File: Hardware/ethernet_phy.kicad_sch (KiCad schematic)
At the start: 28 parts, among them J5 WE-RJ45_7499010211A, U5 DP83822IRHBR

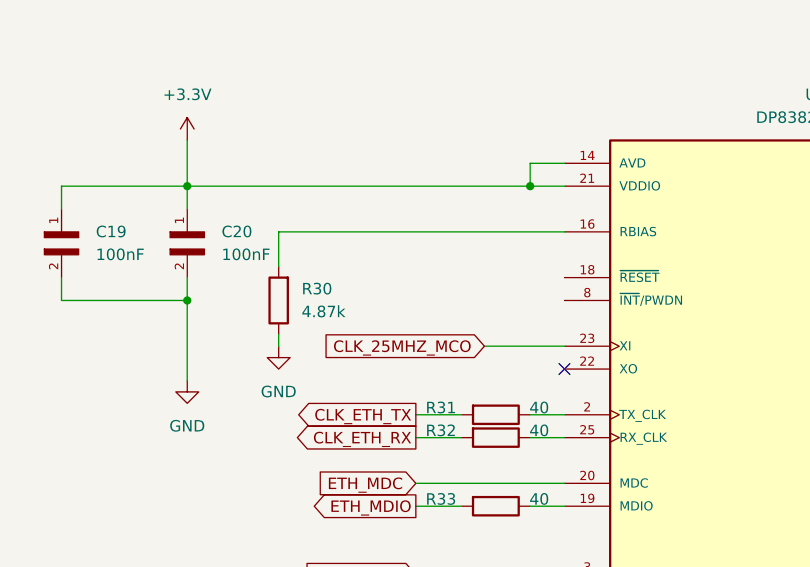
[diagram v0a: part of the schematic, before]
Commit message: Added oscillators, reset button, and finalized ETH connection
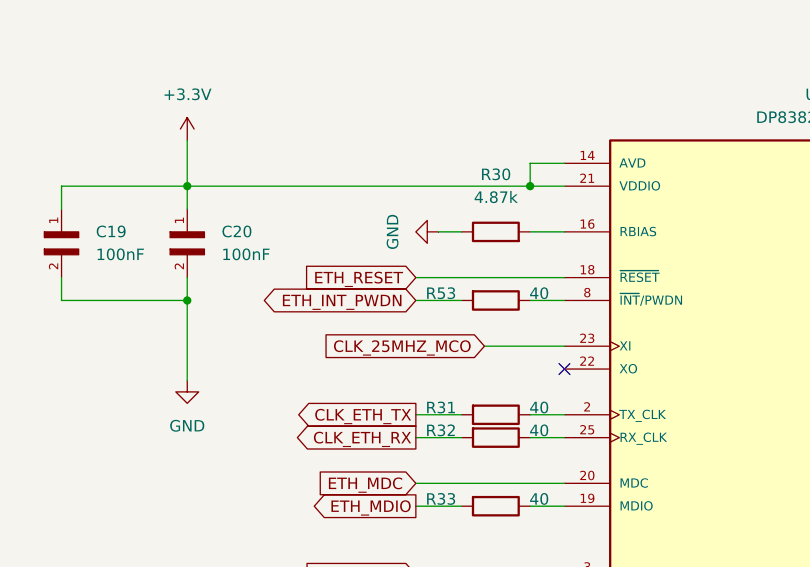
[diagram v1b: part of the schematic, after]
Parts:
- added R53: 40, Resistor_SMD:R_0402_1005Metric, symbol Device:R
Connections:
- net ETH_RESET: now reaches U5.18 (~{RESET})
- net at U5.8 (~{INT}/PWDN): now also R53.1
- new net ETH_INT_PWDN: R53.2
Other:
- company: (none) -> Thomas Montano
- title: (none) -> Ethernet PHY Interface
- moved on the sheet: R30
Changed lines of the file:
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@@
 	(generator_version "9.0")
 	(paper "A4")
+	(title_block
+		(title "Ethernet PHY Interface")
+		(date "2025-06-25")
+		(rev "1")
+		(company "Thomas Montano")
+	)
 	(text "Bias Resistor Connection: A 4.87-kΩ ±1% resistor must be connected \nfrom RBIAS to GND."
 		(exclude_from_sim no)
@@
 	(wire
 		(pts
-			(xy 134.62 123.19) (xy 134.62 125.73)
+			(xy 57.15 54.61) (xy 73.66 54.61)
 		)
 		(stroke
@@
 	(wire
 		(pts
-			(xy 41.91 60.96) (xy 41.91 62.23)
+			(xy 134.62 123.19) (xy 134.62 125.73)
 		)
 		(stroke
@@
 	(wire
 		(pts
+			(xy 69.85 57.15) (xy 73.66 57.15)
+		)
+		(stroke
+			(width 0)
+			(type default)
+		)
+	)
+	(wire
+		(pts
 			(xy 227.33 74.93) (xy 227.33 80.01)
 		)
@@
 	(wire
 		(pts
-			(xy 134.62 133.35) (xy 134.62 137.16)
+			(xy 62.23 49.53) (xy 59.69 49.53)
 		)
 		(stroke
@@
 	(wire
 		(pts
-			(xy 163.83 62.23) (xy 163.83 45.72)
+			(xy 134.62 133.35) (xy 134.62 137.16)
 		)
 		(stroke
@@
 	(wire
 		(pts
-			(xy 129.54 50.8) (xy 148.59 50.8)
+			(xy 163.83 62.23) (xy 163.83 45.72)
 		)
 		(stroke
@@
 	(wire
 		(pts
-			(xy 129.54 53.34) (xy 142.24 53.34)
+			(xy 129.54 50.8) (xy 148.59 50.8)
 		)
 		(stroke
@@
 	(wire
 		(pts
-			(xy 270.51 83.82) (xy 274.32 83.82)
+			(xy 129.54 53.34) (xy 142.24 53.34)
 		)
 		(stroke
@@
 	(wire
 		(pts
-			(xy 163.83 38.1) (xy 163.83 43.18)
+			(xy 270.51 83.82) (xy 274.32 83.82)
 		)
 		(stroke
@@
 	(wire
 		(pts
-			(xy 57.15 97.79) (xy 73.66 97.79)
+			(xy 163.83 38.1) (xy 163.83 43.18)
 		)
 		(stroke
@@
 	(wire
 		(pts
-			(xy 134.62 130.81) (xy 134.62 133.35)
+			(xy 57.15 97.79) (xy 73.66 97.79)
 		)
 		(stroke
@@
 	(wire
 		(pts
-			(xy 41.91 53.34) (xy 41.91 49.53)
+			(xy 134.62 130.81) (xy 134.62 133.35)
 		)
 		(stroke
@@
 	(wire
 		(pts
+			(xy 57.15 57.15) (xy 62.23 57.15)
+		)
+		(stroke
+			(width 0)
+			(type default)
+		)
+	)
+	(wire
+		(pts
 			(xy 73.66 44.45) (xy 69.85 44.45)
 		)
@@
 	(wire
 		(pts
-			(xy 41.91 49.53) (xy 73.66 49.53)
+			(xy 69.85 49.53) (xy 73.66 49.53)
 		)
 		(stroke
@@
 		)
 	)
+	(global_label "ETH_INT_PWDN"
+		(shape bidirectional)
+		(at 57.15 57.15 180)
+		(fields_autoplaced yes)
+		(effects
+			(font
+				(size 1.27 1.27)
+			)
+			(justify right)
+		)
+		(property "Intersheetrefs" "${INTERSHEET_REFS}"
+			(at 45.7587 57.15 0)
+			(effects
+				(font
+					(size 1.27 1.27)
+				)
+				(justify right)
+				(hide yes)
+			)
+		)
+	)
 	(global_label "ETH_RX_CRS"
 		(shape output)
@@
 		)
 	)
+	(global_label "ETH_RESET"
+		(shape input)
+		(at 57.15 54.61 180)
+		(fields_autoplaced yes)
+		(effects
+			(font
+				(size 1.27 1.27)
+			)
+			(justify right)
+		)
+		(property "Intersheetrefs" "${INTERSHEET_REFS}"
+			(at 45.7587 54.61 0)
+			(effects
+				(font
+					(size 1.27 1.27)
+				)
+				(justify right)
+				(hide yes)
+			)
+		)
+	)
 	(global_label "ETH_RX_D0"
 		(shape output)
@@
 	(symbol
 		(lib_id "power:GND")
-		(at 41.91 62.23 0)
+		(at 59.69 49.53 270)
 		(unit 1)
 		(exclude_from_sim no)
@@
 		(dnp no)
 		(property "Reference" "#PWR036"
-			(at 41.91 68.58 0)
+			(at 53.34 49.53 0)
 			(effects
 				(font
@@
 		)
 		(property "Value" "GND"
-			(at 41.91 67.31 0)
+			(at 54.61 49.53 0)
 			(effects
 				(font
@@
 		)
 		(property "Footprint" ""
-			(at 41.91 62.23 0)
+			(at 59.69 49.53 0)
 			(effects
 				(font
@@
 		)
 		(property "Datasheet" ""
-			(at 41.91 62.23 0)
+			(at 59.69 49.53 0)
 			(effects
 				(font
@@
 		)
 		(property "Description" "Power symbol creates a global label with name \"GND\" , ground"
-			(at 41.91 62.23 0)
+			(at 59.69 49.53 0)
 			(effects
 				(font
@@
 	(symbol
 		(lib_id "Device:R")
-		(at 41.91 57.15 180)
+		(at 66.04 49.53 90)
 		(unit 1)
 		(exclude_from_sim no)
@@
 		(fields_autoplaced yes)
 		(property "Reference" "R30"
-			(at 44.45 55.8799 0)
+			(at 66.04 43.18 90)
 			(effects
 				(font
 					(size 1.27 1.27)
 				)
-				(justify right)
 			)
 		)
 		(property "Value" "4.87k"
-			(at 44.45 58.4199 0)
+			(at 66.04 45.72 90)
 			(effects
 				(font
 					(size 1.27 1.27)
 				)
-				(justify right)
 			)
 		)
 		(property "Footprint" "Resistor_SMD:R_0402_1005Metric"
-			(at 43.688 57.15 90)
+			(at 66.04 51.308 90)
 			(effects
 				(font
@@
 		)
 		(property "Datasheet" "~"
-			(at 41.91 57.15 0)
+			(at 66.04 49.53 0)
 			(effects
 				(font
@@
 		)
 		(property "Description" "Resistor"
-			(at 41.91 57.15 0)
+			(at 66.04 49.53 0)
 			(effects
 				(font
@@
 					(unit 1)
 				)
+			)
+		)
+	)
+	(symbol
+		(lib_id "Device:R")
+		(at 66.04 57.15 270)
+		(unit 1)
+		(exclude_from_sim no)
+		(in_bom yes)
+		(on_board yes)
+		(dnp no)
+		(property "Reference" "R53"
+			(at 59.944 56.388 90)
+			(effects
+				(font
+					(size 1.27 1.27)
+				)
+			)
+		)
+		(property "Value" "40"
+			(at 70.866 56.388 90)
+			(effects
+				(font
+					(size 1.27 1.27)
+				)
+			)
+		)
+		(property "Footprint" "Resistor_SMD:R_0402_1005Metric"
+			(at 66.04 55.372 90)
+			(effects
+				(font
+					(size 1.27 1.27)
+				)
+				(hide yes)
+			)
+		)
+		(property "Datasheet" "~"
+			(at 66.04 57.15 0)
+			(effects
+				(font
+					(size 1.27 1.27)
+				)
+				(hide yes)
+			)
+		)
+		(property "Description" "Resistor"
+			(at 66.04 57.15 0)
+			(effects
+				(font
+					(size 1.27 1.27)
+				)
+				(hide yes)
+			)
+		)
+		(pin "1"
+		)
+		(pin "2"
+		)
+		(instances
+			(project "Radio Project"
+				(path "/ca6389fe-9846-40e3-87a4-456cfcfc0777/8127e5c0-6601-4146-a9f2-512dea28772c"
+					(reference "R53")
+					(unit 1)
+				)

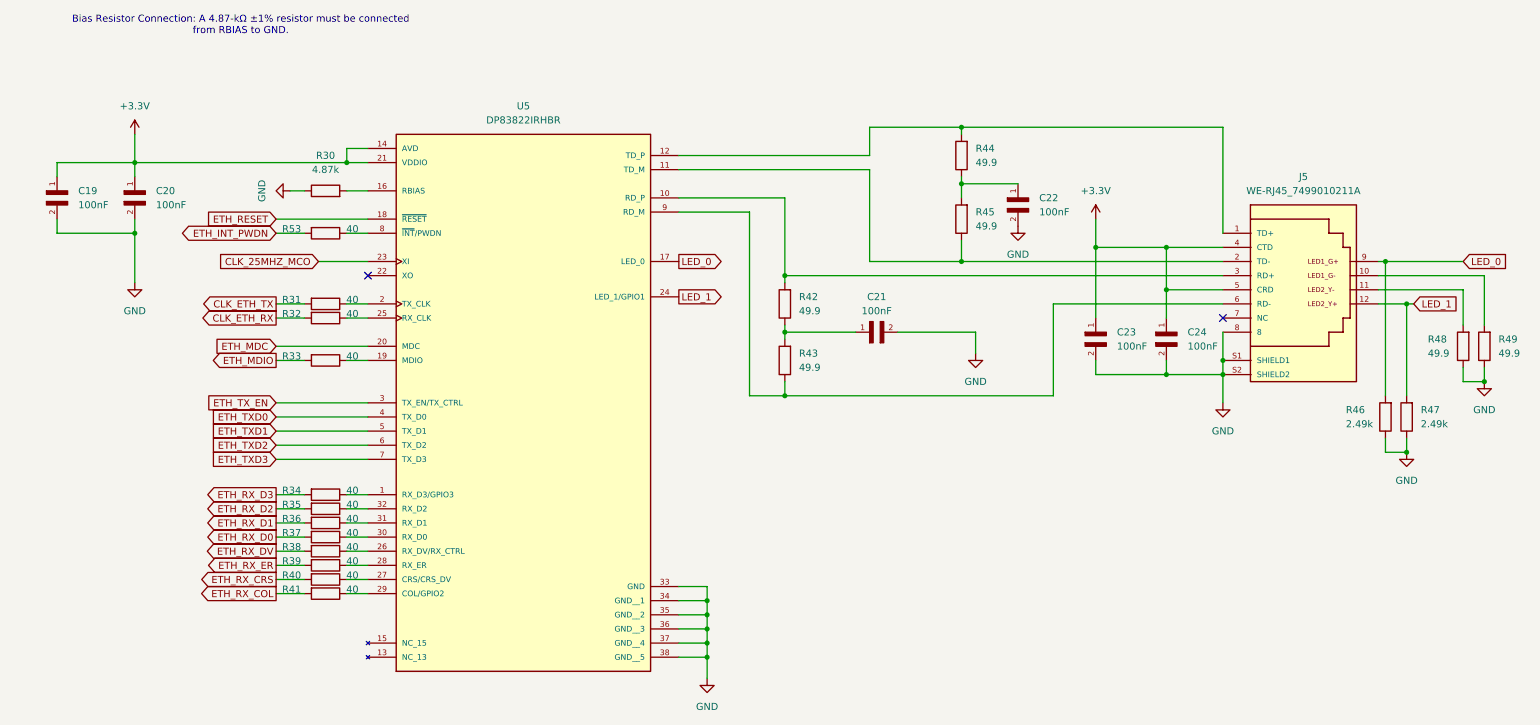
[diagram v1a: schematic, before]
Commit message: changed to SI4468, added 30 MHz oscillators, and connected it to MCU
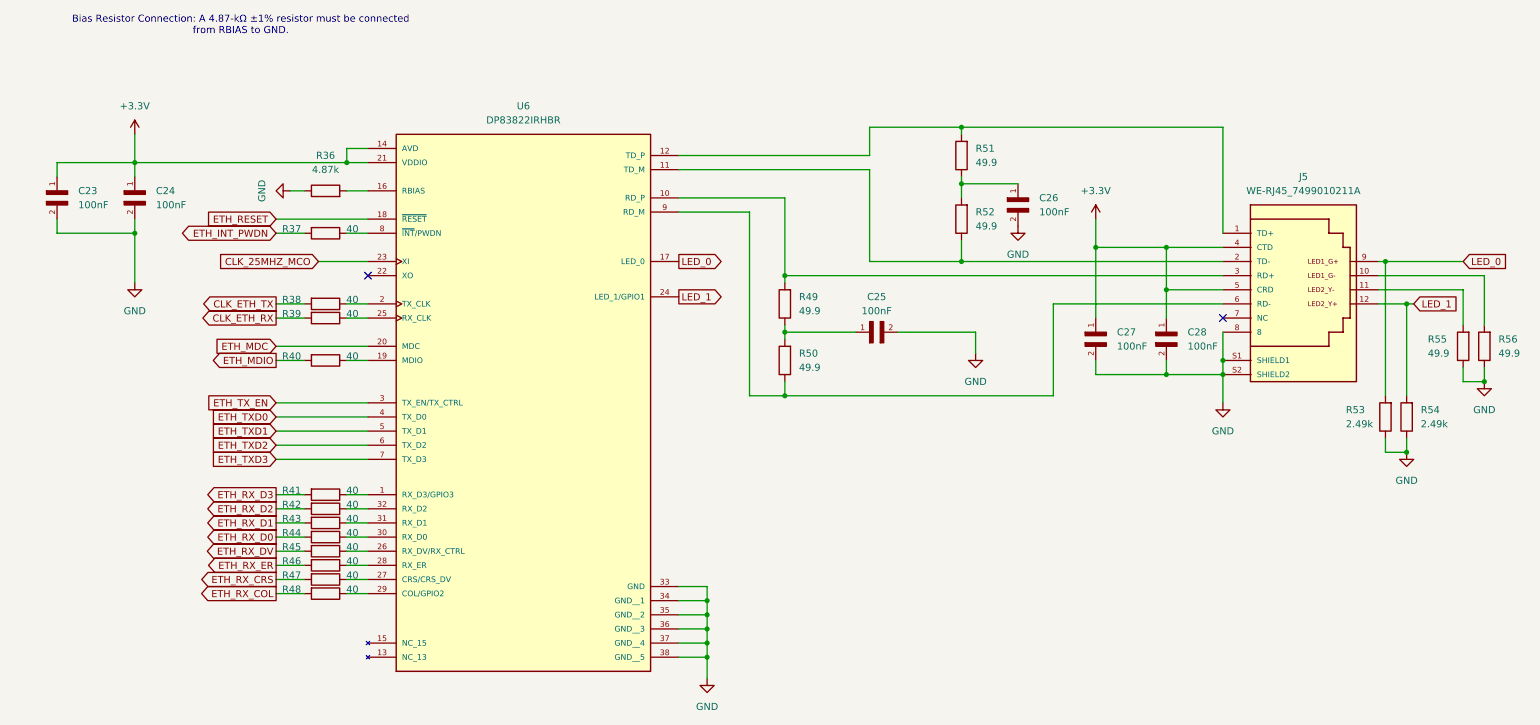
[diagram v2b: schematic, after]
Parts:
- renumbered C19 to C23, C20 to C24, C21 to C25, C22 to C26, C23 to C27, C24 to C28, R30 to R36, R53 to R37, R31 to R38, R32 to R39, R33 to R40, R34 to R41, R35 to R42, R36 to R43, R37 to R44, R38 to R45, R39 to R46, R40 to R47, R41 to R48, R42 to R49, R43 to R50, R44 to R51, R45 to R52, R46 to R53, R47 to R54, R48 to R55, R49 to R56, U5 to U6
